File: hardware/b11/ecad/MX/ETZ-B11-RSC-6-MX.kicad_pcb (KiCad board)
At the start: 2 copper layers, 131.5 x 85.8 mm, 44 parts, among them SW1 MX-Hotswap-1U, SW10 MX-Hotswap-1U, SW11 MX-Hotswap-1U, SW12 MX-Hotswap-1U, SW13 MX-Hotswap-1U, SW14 MX-Hotswap-1U, SW15 MX-Hotswap-1U, SW16 MX-Hotswap-1U, SW17 MX-Hotswap-1U, SW18 MX-Hotswap-1U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

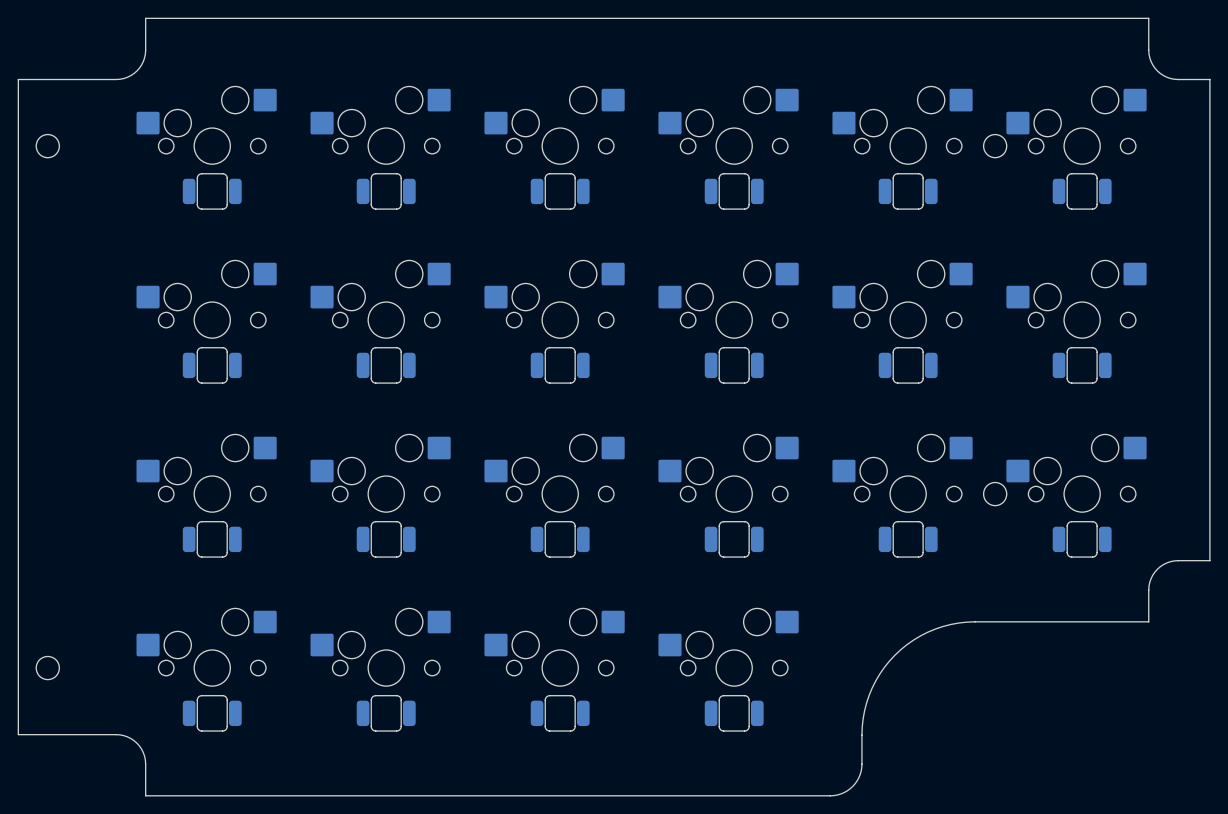
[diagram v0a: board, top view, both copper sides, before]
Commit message: Regenerate B11 PCBs after library cleanup [skip ci]
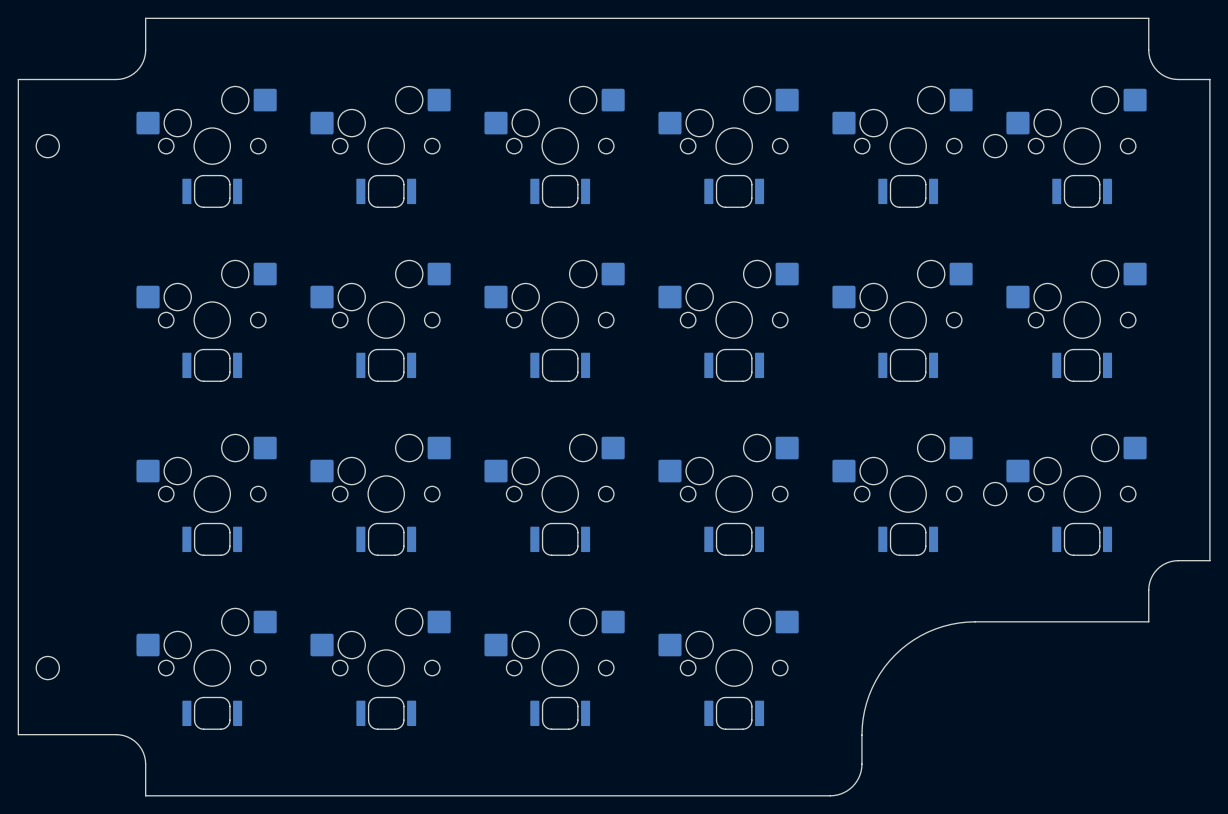
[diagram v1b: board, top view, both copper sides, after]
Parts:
- LED1, LED10, LED11, LED12, LED13, LED14, LED15, LED16, LED17, LED18, LED19, LED2, LED20, LED21, LED22, LED3, LED4, LED5, LED6, LED7, LED8, LED9: value LED_SMD_6028_BackMount -> 6028_LED; footprint LED_SMD_6028_BackMount -> 6028_LED; moved to F.Cu
- SW1, SW10, SW11, SW12, SW13, SW14, SW15, SW16, SW17, SW18, SW19, SW2, SW20, SW21, SW22, SW3, SW4, SW5, SW6, SW7, SW8, SW9: value MX-Hotswap-1U -> PG151101S11; footprint MX-Hotswap-1U -> PG151101S11
